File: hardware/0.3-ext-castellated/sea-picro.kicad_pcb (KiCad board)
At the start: 4 copper layers, 17.8 x 33 mm, 54 parts, among them J1 USB_C_Receptacle_USB2.0, J2 Sea-Picro, Q1 2N7002VC-7, Q2 2N7002VC-7, U1 AP7365-33WG-7, U2 GD25Q64CWIGR, U3 RP2040, U4 74LVC1T45Z6-7, Y1 12MHz

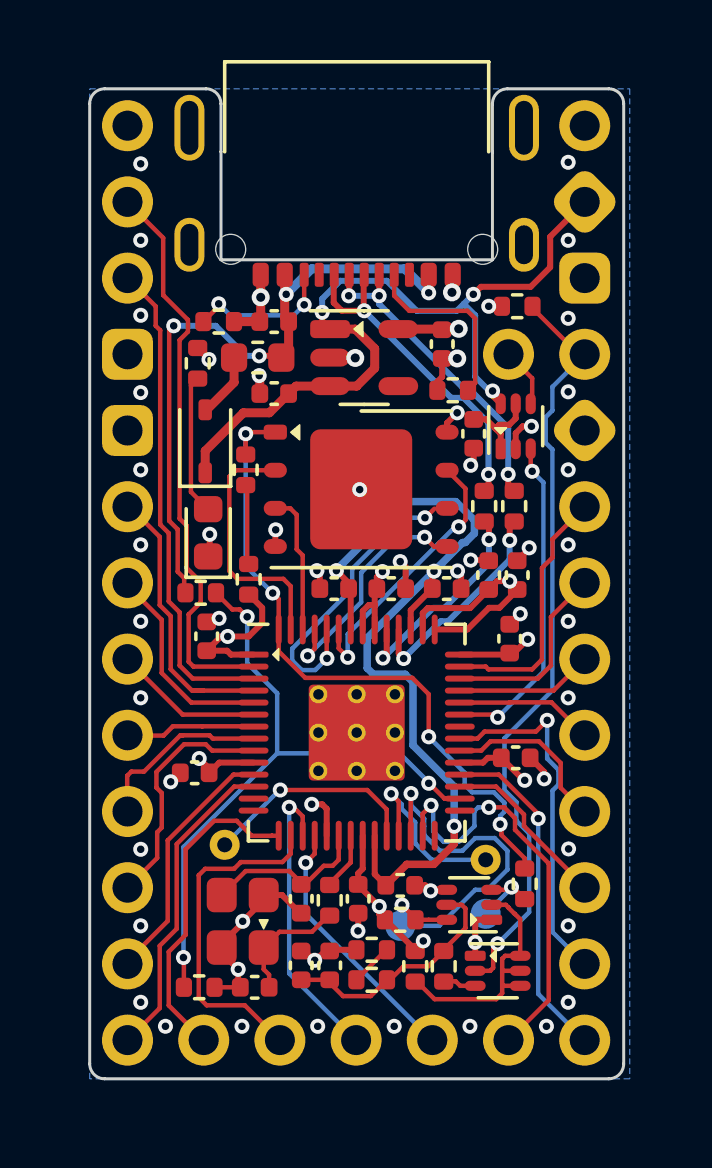
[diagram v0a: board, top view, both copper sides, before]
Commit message: add castellated r0.3, fix gnd pour
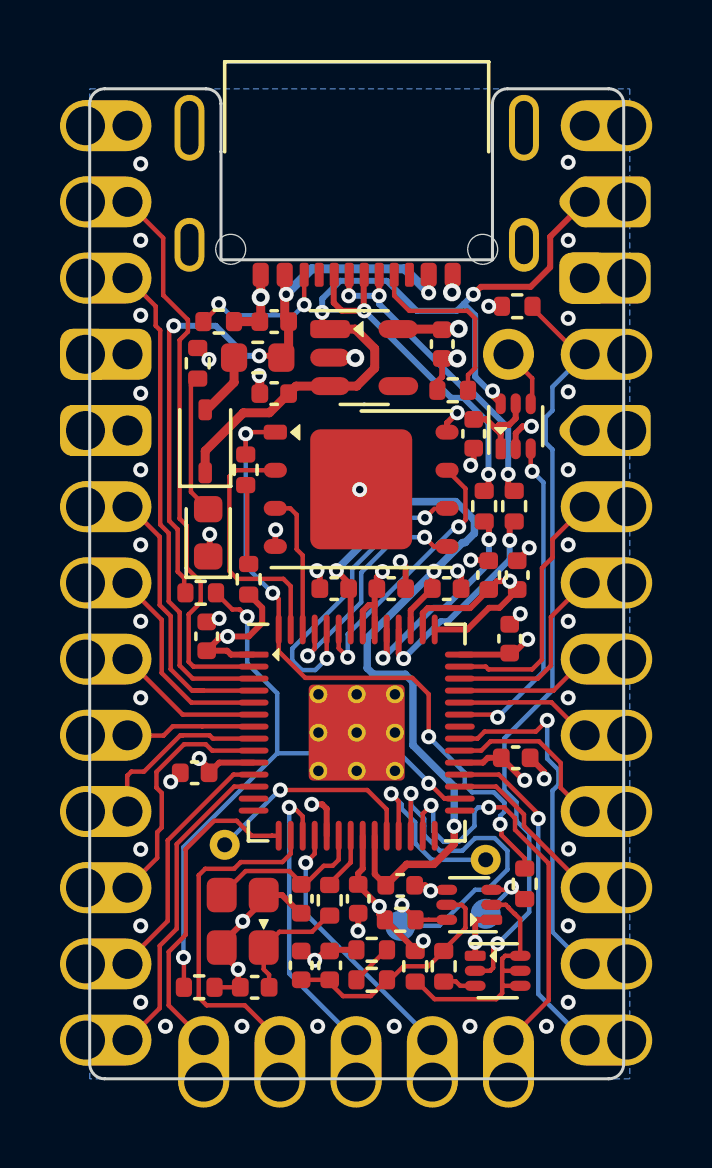
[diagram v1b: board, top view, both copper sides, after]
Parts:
- J2: footprint josh-module:Sea-Picro_EXT_Pins -> josh-module:Sea-Picro_EXT_Pins_Castellated

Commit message: update production outputs
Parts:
- U4: value 74LVC1T45Z6-7 -> 74LVC1T45

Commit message: add teardrops and melted versions, update LDO MPN
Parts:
- U1: value AP7365-33WG-7 -> XC6210B332MR-G
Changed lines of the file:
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@@
     (tags "SOT TO_SOT_SMD")
     (property "JLC Basic" "N")
-    (property "LCSC" "C150742")
-    (property "LCSC2" "C82942")
-    (property "MPN " "AP7365-33WG-7 ")
-    (property "MPN2" "ME6211C33M5G-N")
-    (property "Manufacturer" "Diodes Incorporated")
-    (property "Manufacturer2" "MICRONE(Nanjing Micro One Elec) ")
+    (property "LCSC" "C47719")
+    (property "LCSC2" "")
+    (property "MPN " "XC6210B332MR-G")
+    (property "MPN2" "")
+    (property "Manufacturer" "Torex Semiconductor")
+    (property "Manufacturer2" "")
     (property "Sheetfile" "sea-picro.kicad_sch")
     (property "Sheetname" "")
-    (property "Substitute" "Y - Confirm with Josh")
+    (property "Substitute" "N")
     (attr smd)
     (fp_text reference "U1" (at 0 -2.4) (layer "F.SilkS") hide
       (effects (font (size 1 1) (thickness 0.15)))
     )
-    (fp_text value "AP7365-33WG-7 " (at 0 2.4) (layer "F.Fab")
+    (fp_text value "XC6210B332MR-G" (at 0 2.4) (layer "F.Fab")
       (effects (font (size 1 1) (thickness 0.15)))
     )
